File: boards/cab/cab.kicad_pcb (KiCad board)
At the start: 2 copper layers, 71.3 x 71.3 mm, 44 parts, among them J1 Conn_01x08_Female, J2 Conn_01x08_Female, J3 Conn_01x08_Female, J4 Conn_01x08_Female, Q1 SI2308A, Q2 S8550, Q3 BC817-40,215, Q4 S8550, Q5 BC817-40,215, Q6 S8550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

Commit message: Created PCB
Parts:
- removed the Q4 at (229.1, 37.4)
- removed the Q4 at (228.5, 47.9)
- removed the Q6 at (202.0, 71.7)
- removed the Q6 at (238.9, 37.4)
- removed the Q8 at (234.0, 37.4)
- removed the Q8 at (216.9, 59.5)
- removed the U1 at (241.0, 47.2)
- removed the U1 at (247.4, 45.7)
- removed the U2 at (202.9, 77.0)
- removed the U2 at (238.9, 45.7)
- added Q4: S8550, Package_TO_SOT_SMD:SOT-23, F.Cu at (231.9, 145.4)
- added Q6: S8550, Package_TO_SOT_SMD:SOT-23, F.Cu at (237.4, 145.3)
- added Q8: S8550, Package_TO_SOT_SMD:SOT-23, F.Cu at (243.1, 144.9)
- added R10: 50k, Resistor_SMD:R_0805_2012Metric, F.Cu at (192.0, 146.0)
- added R11: 4.7k, Resistor_SMD:R_0805_2012Metric, F.Cu at (177.5, 145.1)
- added SW1: SW_Push, Connector_PinHeader_2.54mm:PinHeader_1x02_P2.54mm_Vertical, F.Cu at (191.1, 151.7)
- added U1: XL1509-ADJ, Package_SO:SOIC-8_3.9x4.9mm_P1.27mm, F.Cu at (236.5, 114.2)
- added U2: XL1509-5.0, Package_SO:SOIC-8_3.9x4.9mm_P1.27mm, F.Cu at (98.4, 44.7)
- L3: footprint StackCabinet:Solenoid -> TerminalBlock_4Ucon:TerminalBlock_4Ucon_1x02_P3.50mm_Vertical
- Q2, Q3, Q5, Q7: footprint Package_TO_SOT_THT:TO-220-3_Vertical -> Package_TO_SOT_SMD:SOT-23
- moved C4 125.2 mm to (100.5, 53.0)
- moved C9 118.9 mm to (171.8, 147.8)
- moved R4 112.4 mm to (239.9, 162.0)
- moved Q7 111.4 mm to (244.9, 157.6)
- moved R5 107.5 mm to (245.4, 162.4)
- moved U3 99.0 mm to (177.4, 150.9)
- moved C2 92.9 mm to (113.5, 44.1), turned to 180 degrees
- moved C8 91.1 mm to (171.9, 151.0)
- moved R3 87.7 mm to (233.1, 162.1)
- moved R6 86.2 mm to (226.7, 149.8)
- moved Q5 85.7 mm to (238.1, 157.4)
- moved C6 84.5 mm to (144.7, 43.6)
- moved R8 82.7 mm to (237.5, 149.3)
- moved Q3 82.5 mm to (233.0, 157.0)
- moved R9 80.0 mm to (243.0, 149.1)
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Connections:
- U3 pad 10: unconnected-(U3-Pad10) -> CAB_STATE
- U3 pad 11: unconnected-(U3-Pad11) -> RxD
- U3 pad 12: unconnected-(U3-Pad12) -> TxD
- U3 pad 13: unconnected-(U3-Pad13) -> 24V_EN
- U3 pad 19: unconnected-(U3-Pad19) -> Net-(U3-Pad19)

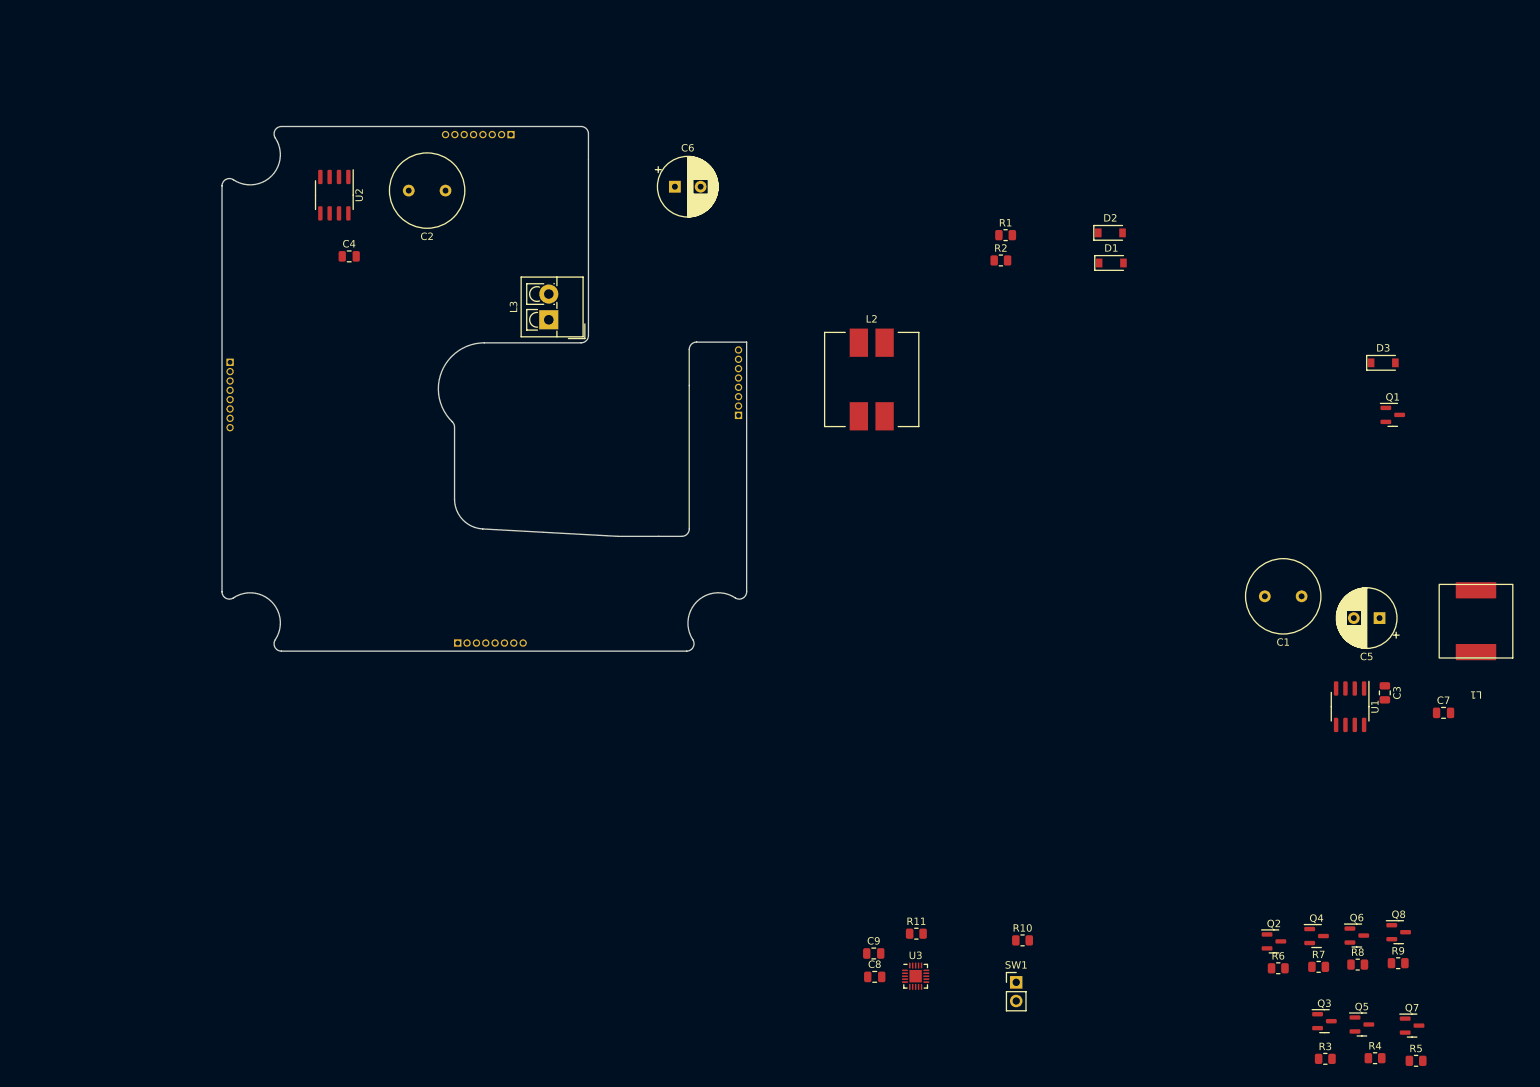
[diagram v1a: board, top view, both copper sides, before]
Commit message: Reworked board outline
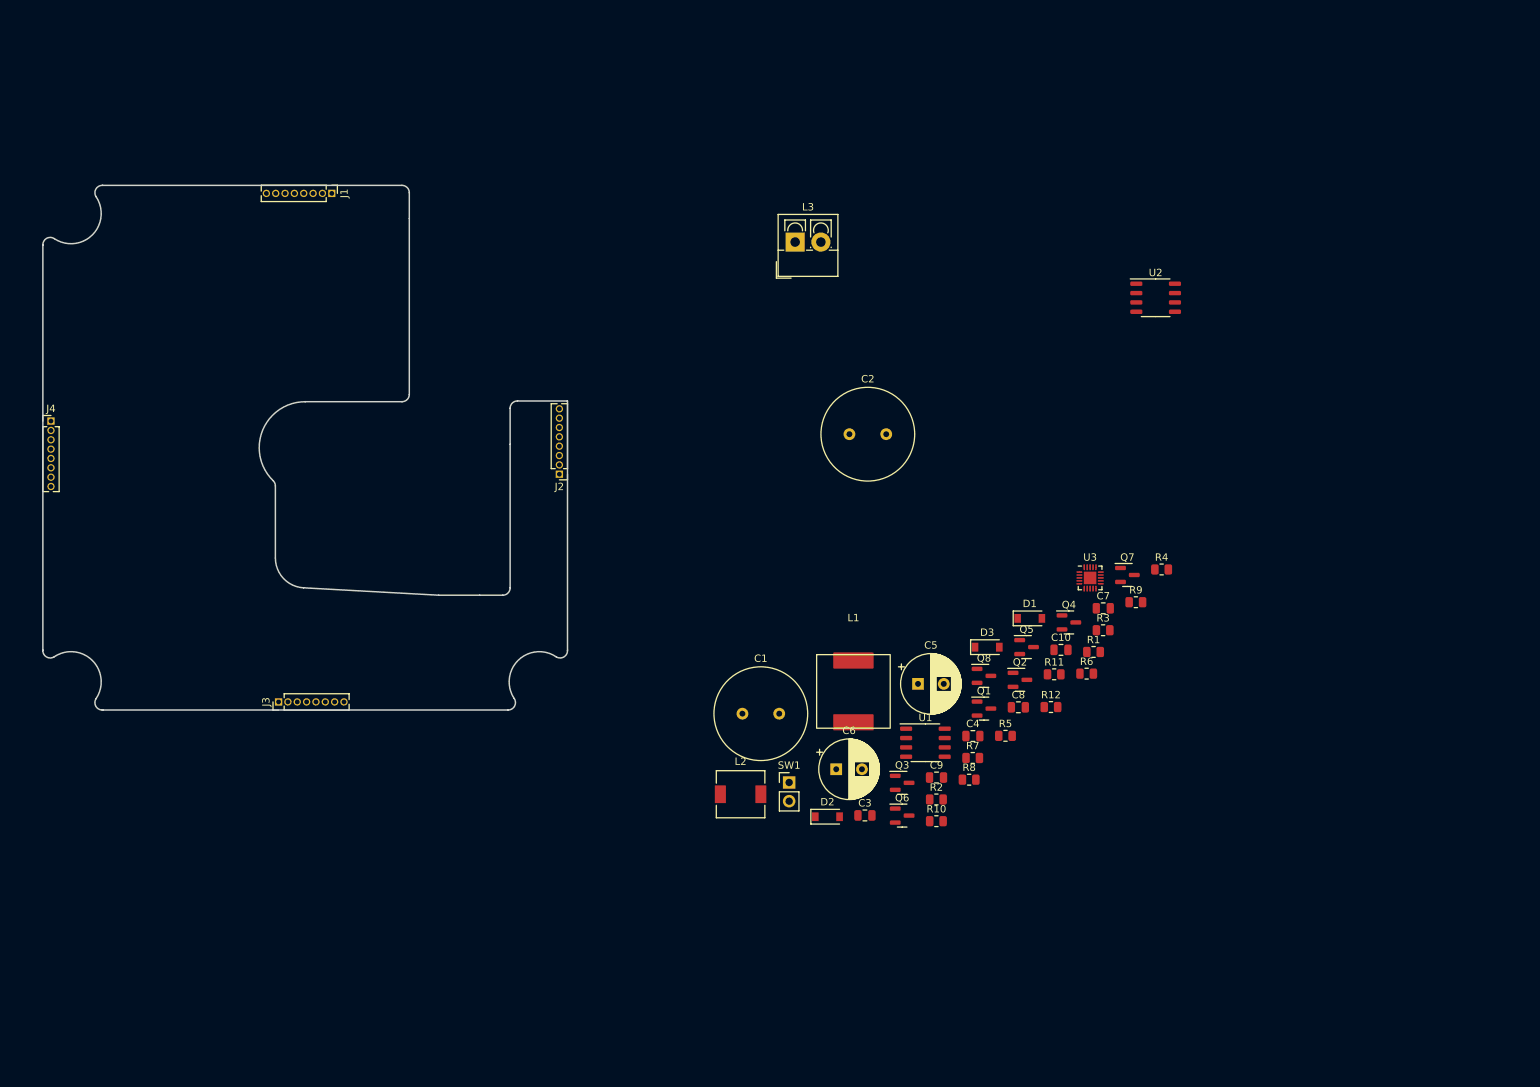
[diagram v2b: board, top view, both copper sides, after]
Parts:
- added C10: 0.1uF, Capacitor_SMD:C_0805_2012Metric, F.Cu at (197.2, 106.5)
- added R12: 1k, Resistor_SMD:R_0805_2012Metric, F.Cu at (195.8, 114.3)
- C1, C2: footprint Capacitor_THT:C_Radial_D10.0mm_H16.0mm_P5.00mm -> Capacitor_THT:C_Radial_D12.5mm_H20.0mm_P5.00mm
- J1, J2, J3, J4: moved to F.Cu
- L2: footprint Inductor_SMD:L_Wuerth_WE-DD-Typ-L-Typ-XL-Typ-XXL -> Inductor_SMD:L_6.3x6.3_H3
- R1: value 50k -> 2.7k
- R2: value 2.7k -> 50k
- U1, U2: footprint Package_SO:SOIC-8_3.9x4.9mm_P1.27mm -> Package_SO:SOP-8_3.9x4.9mm_P1.27mm
- moved U2 112.5 mm to (210.1, 58.7), turned to 0 degrees
- moved C4 106.9 mm to (185.2, 118.2)
- moved D2 88.2 mm to (165.4, 129.2)
- moved L1 85.1 mm to (169.0, 112.2), turned to 0 degrees
- moved C6 82.1 mm to (166.6, 122.8)
- moved C1 77.7 mm to (153.9, 115.2), turned to 0 degrees
- moved R2 73.8 mm to (180.3, 126.9)
- moved C3 72.6 mm to (170.6, 129.0), turned to 0 degrees
- moved R4 72.5 mm to (210.9, 95.6)
- moved Q7 72.4 mm to (206.2, 96.3)
- moved R5 71.2 mm to (189.7, 118.2)
- moved Q5 68.6 mm to (192.5, 106.2)
- moved Q1 68.4 mm to (186.7, 114.5)
- moved D3 66.3 mm to (187.2, 106.2)
- moved Q8 66.3 mm to (186.7, 110.1)
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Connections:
- D2 pad 1: Net-(D2-Pad1) -> 24V
- D2 pad 2: GND -> Net-(D2-Pad2)
- D3 pad 1: 24V -> Net-(D3-Pad1)
- D3 pad 2: Net-(D3-Pad2) -> GND
- L2 pad 1: Net-(D2-Pad1) -> Net-(D3-Pad1)
- L3 pad 2: Net-(D3-Pad2) -> Net-(D2-Pad2)
- Q1 pad 1: SOL_EN -> Net-(Q1-Pad1)
- Q1 pad 3: Net-(D3-Pad2) -> Net-(D2-Pad2)
- Q4 pad 1: Net-(R7-Pad2) -> Net-(Q4-Pad1)
- Q8 pad 1: Net-(R9-Pad2) -> Net-(Q8-Pad1)
- R1 pad 1: FB -> GND
- R1 pad 2: 5V -> FB
- R2 pad 1: GND -> FB
- R2 pad 2: FB -> 5V
- R3 pad 1: R_PWM -> SOL_EN
- R3 pad 2: Net-(Q3-Pad1) -> Net-(Q1-Pad1)
- R4 pad 1: G_PWM -> R_PWM
- R4 pad 2: Net-(Q5-Pad1) -> Net-(Q3-Pad1)
- R5 pad 1: B_PWM -> LED1_PWM
- R5 pad 2: Net-(Q7-Pad1) -> Net-(Q4-Pad1)
- R7 pad 1: LED1_PWM -> G_PWM
- R7 pad 2: Net-(R7-Pad2) -> Net-(Q5-Pad1)
- R9 pad 1: LED3_PWM -> B_PWM
- R9 pad 2: Net-(R9-Pad2) -> Net-(Q7-Pad1)
- U2 pad 2: Net-(D2-Pad1) -> Net-(D3-Pad1)
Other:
- outline, holes or cut-outs redrawn

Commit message: Fixed mosfet footprint
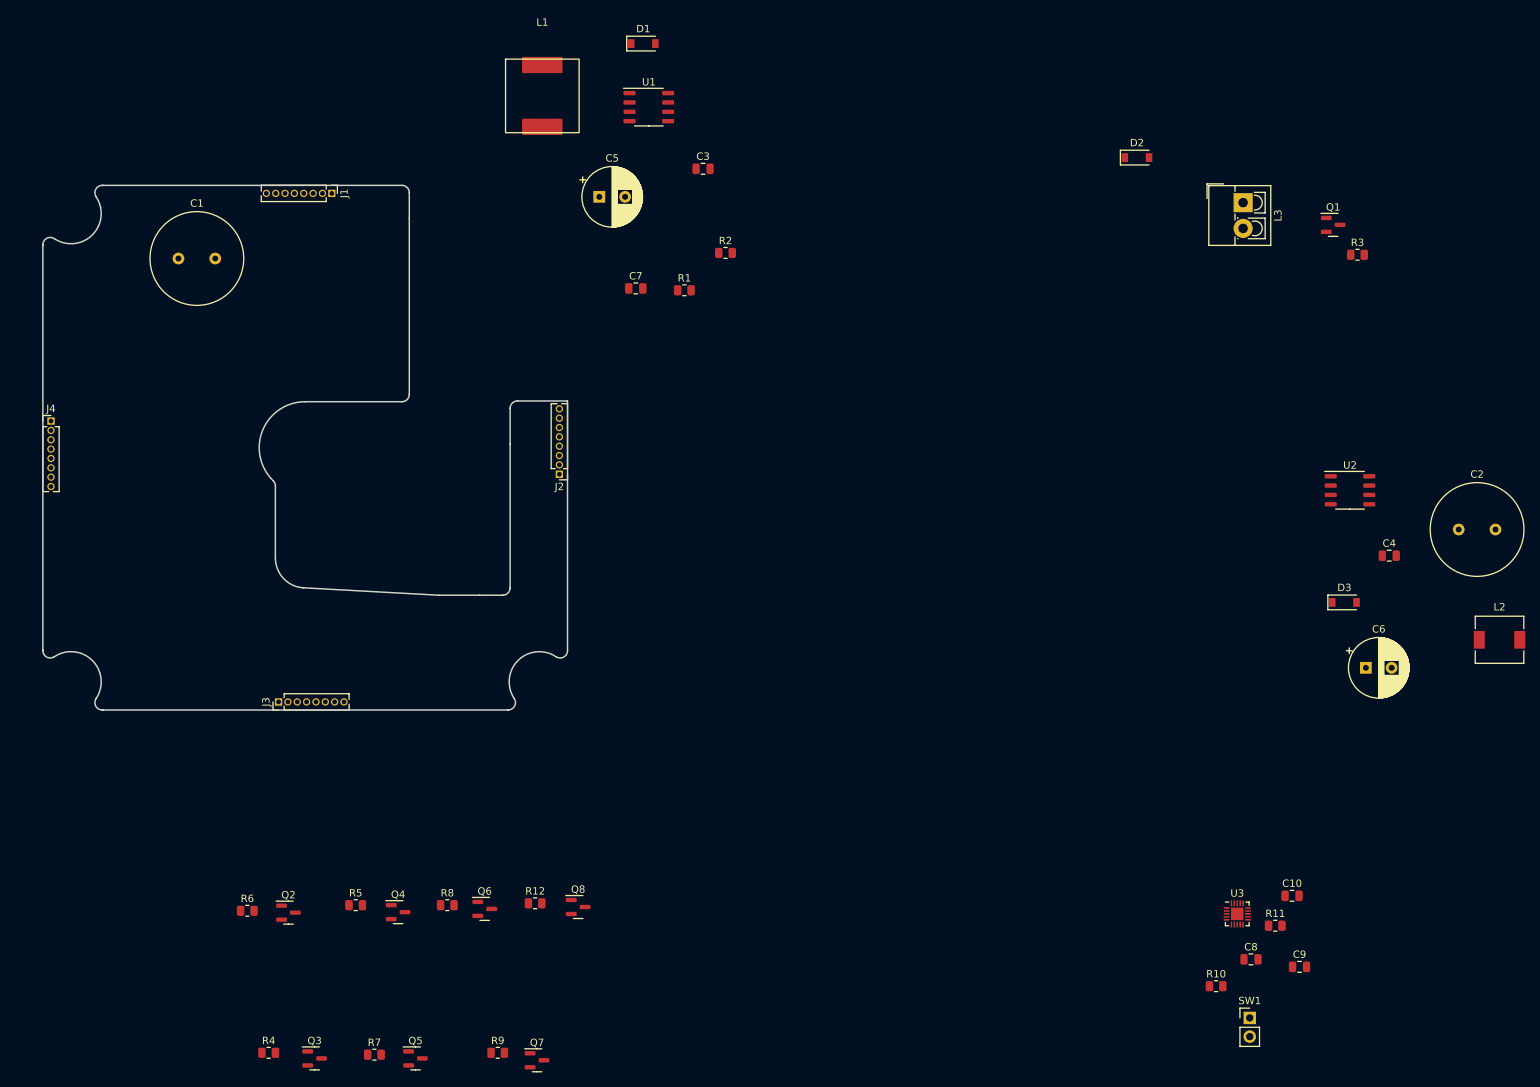
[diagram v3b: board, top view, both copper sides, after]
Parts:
- moved R4 138.0 mm to (89.5, 161.3)
- moved R6 118.5 mm to (86.6, 142.0)
- moved R9 106.2 mm to (120.7, 161.3)
- moved L2 105.3 mm to (256.8, 105.2)
- moved Q2 104.3 mm to (92.2, 142.2)
- moved Q7 103.9 mm to (126.0, 162.3)
- moved Q5 100.1 mm to (109.5, 162.1)
- moved Q4 99.3 mm to (107.1, 142.2)
- moved D2 99.0 mm to (207.5, 39.6)
- moved C1 98.5 mm to (77.3, 53.3)
- moved U1 94.2 mm to (141.2, 32.8)
- moved D1 94.1 mm to (140.4, 24.1)
- moved L1 91.3 mm to (126.7, 31.2)
- moved R5 91.3 mm to (101.3, 141.2)
- moved R7 90.8 mm to (103.9, 161.5)
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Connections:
- Q2 pad 2: LED0 -> 5V
- Q2 pad 3: 5V -> LED0
- Q4 pad 2: LED1 -> 5V
- Q4 pad 3: 5V -> LED1
- Q6 pad 2: LED2 -> 5V
- Q6 pad 3: 5V -> LED2
- Q8 pad 2: LED3 -> 5V
- Q8 pad 3: 5V -> LED3

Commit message: Placed Power, Attiny and LED power
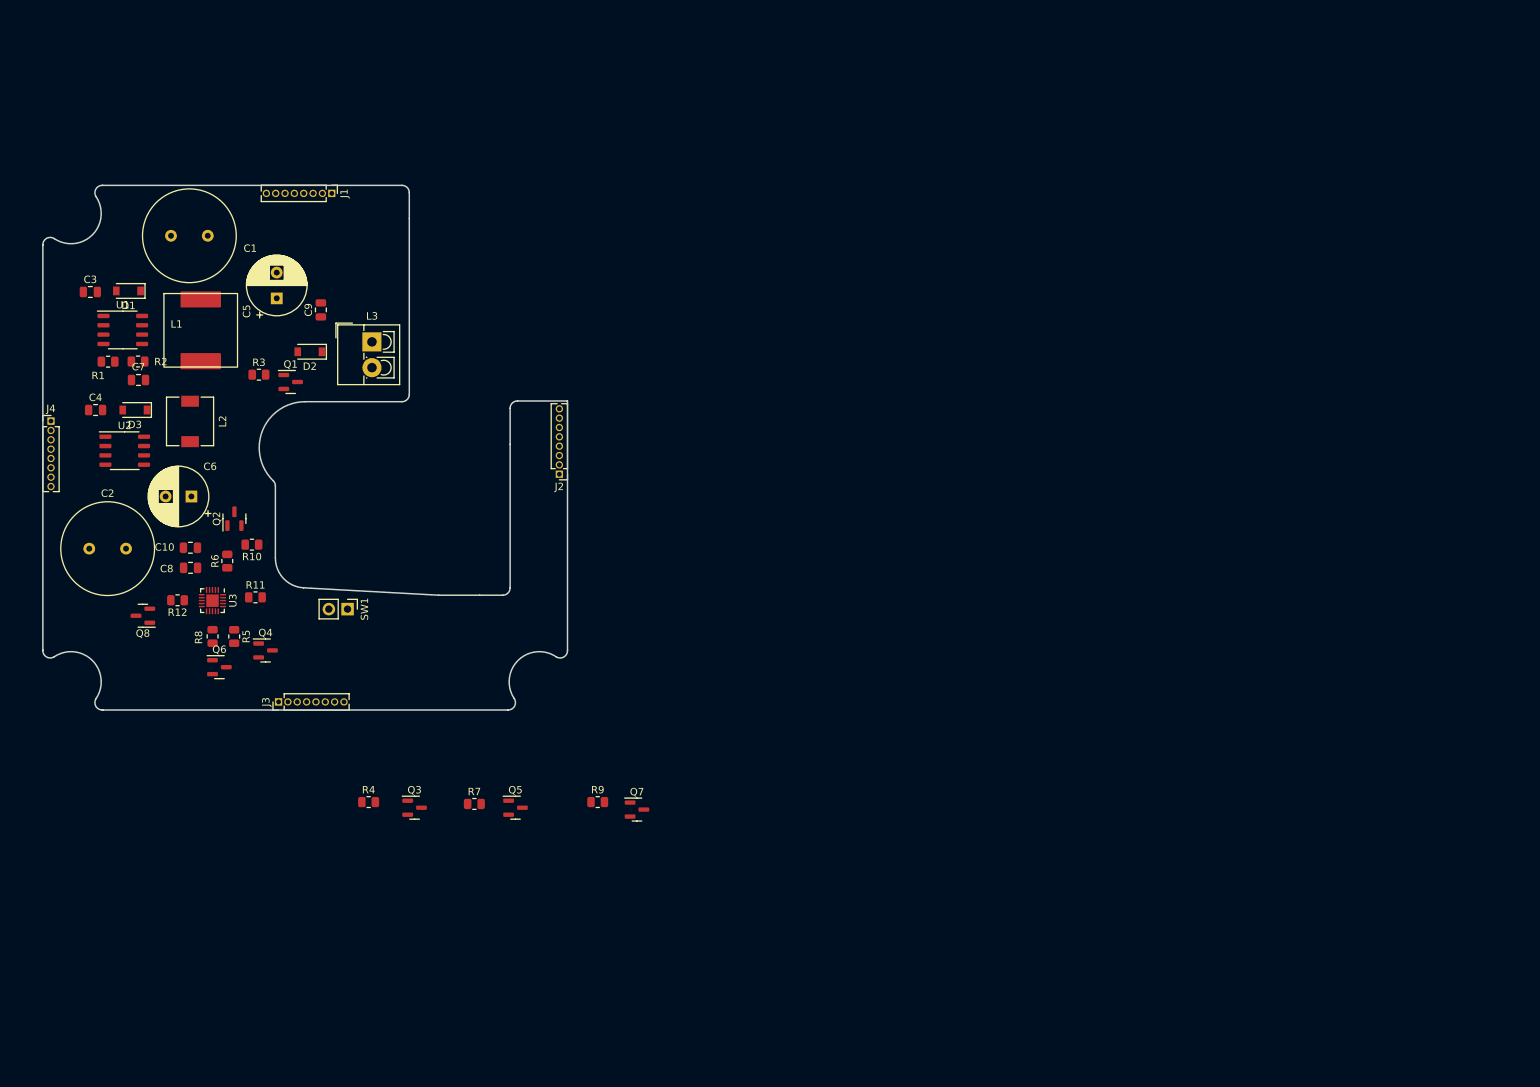
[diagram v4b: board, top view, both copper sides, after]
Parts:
- moved C2 186.1 mm to (65.1, 92.8)
- moved L2 180.4 mm to (78.8, 75.5), turned to -90 degrees
- moved C4 176.9 mm to (66.0, 73.9)
- moved U2 166.6 mm to (70.0, 79.5)
- moved D3 166.4 mm to (71.3, 73.9), turned to 180 degrees
- moved C6 161.3 mm to (79.0, 85.7), turned to 180 degrees
- moved C9 160.2 mm to (96.6, 60.3), turned to 90 degrees
- moved C10 157.0 mm to (78.9, 92.7), turned to 180 degrees
- moved C8 153.6 mm to (78.9, 95.4), turned to 180 degrees
- moved R3 150.2 mm to (88.2, 69.1)
- moved U3 145.6 mm to (81.9, 99.8), turned to -90 degrees
- moved R11 145.6 mm to (87.7, 99.4)
- moved R10 144.1 mm to (87.2, 92.2), turned to 180 degrees
- moved Q1 143.3 mm to (92.5, 70.1)
- moved SW1 134.6 mm to (100.2, 101.0), turned to -90 degrees
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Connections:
- C5 pad 1: 5V -> 24V
- C6 pad 1: 24V -> 5V
- C7 pad 1: 5V -> 24V
- L1 pad 2: 5V -> 24V
- L2 pad 2: 24V -> 5V
- R2 pad 2: 5V -> 24V
- U2 pad 3: 24V -> 5V
- U3 pad 1: R_PWM -> SOL_EN
- U3 pad 12: TxD -> GDA
- U3 pad 13: 24V_EN -> LED2_PWM
- U3 pad 14: SOL_EN -> LED1_PWM
- U3 pad 2: G_PWM -> 24V_EN
- U3 pad 6: LED1_PWM -> R_PWM
- U3 pad 7: LED2_PWM -> G_PWM

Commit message: Routing & planes
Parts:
- moved Q7 64.7 mm to (78.8, 105.8), turned to -90 degrees
- moved R9 61.0 mm to (79.0, 101.4), turned to -90 degrees
- moved Q5 44.4 mm to (84.6, 105.9), turned to -90 degrees
- moved Q3 42.3 mm to (73.3, 105.8), turned to -90 degrees
- moved R7 41.9 mm to (84.7, 101.4), turned to -90 degrees
- moved R4 39.4 mm to (73.4, 101.4), turned to -90 degrees
- moved SW1 30.7 mm to (96.9, 70.5)
- moved Q2 15.5 mm to (76.2, 101.6), turned to -90 degrees
- moved R11 11.6 mm to (88.5, 87.8), turned to 90 degrees
- moved R10 9.62 mm to (78.4, 88.5), turned to 90 degrees
- moved R6 8.70 mm to (76.2, 98.5), turned to 0 degrees
- moved C8 8.57 mm to (82.0, 87.4), turned to 0 degrees
- moved Q6 7.35 mm to (81.8, 101.6), turned to -90 degrees
- moved U3 6.90 mm to (81.9, 92.9)
- moved R5 6.73 mm to (87.5, 98.5), turned to 0 degrees
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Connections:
- net Net-(D2-Pad2) renamed /SOL_R
- U3 pad 1: SOL_EN -> 24V_EN
- U3 pad 10: CAB_STATE -> LED2_PWM
- U3 pad 13: LED2_PWM -> G_PWM
- U3 pad 2: 24V_EN -> unconnected-(U3-Pad2)
- U3 pad 20: LED0_PWM -> SOL_EN
- U3 pad 5: B_PWM -> CAB_STATE
- U3 pad 6: R_PWM -> LED3_PWM
- U3 pad 7: G_PWM -> R_PWM
- U3 pad 8: LED3_PWM -> LED0_PWM
- U3 pad 9: unconnected-(U3-Pad9) -> B_PWM
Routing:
- net G: track 0.00 -> 179.1 mm, vias 0 -> 3
- net B: track 0.00 -> 178.4 mm, vias 0 -> 4
- net R: track 0.00 -> 177.6 mm, vias 0 -> 3
- net GDA: track 0.00 -> 175.3 mm, vias 0 -> 4
- net LED0: track 0.00 -> 85.0 mm, vias 0 -> 4
- net SEL1: track 0.00 -> 70.1 mm, vias 0 -> 2
- net LED1: track 0.00 -> 63.5 mm, vias 0 -> 3
- net SEL0: track 0.00 -> 58.2 mm, vias 0 -> 1
- net 5V: track 0.00 -> 53.9 mm, vias 0 -> 7
- net 24V_EN: track 0.00 -> 47.8 mm, vias 0 -> 2
- net CAB_STATE: track 0.00 -> 37.8 mm, vias 0 -> 2
- net LED3: track 0.00 -> 36.6 mm, vias 0 -> 2
- net SEL3: track 0.00 -> 36.4 mm, vias 0 -> 2
- net SOL_EN: track 0.00 -> 29.0 mm
- net SEL2: track 0.00 -> 27.9 mm, vias 0 -> 2
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- added copper zone on F.Cu, net /SOL_R
- added copper zone on F.Cu, net 24V
- added copper zone on F.Cu, net 5V
- added copper zone on B.Cu, net GND
- added copper zone on F.Cu, net GND
- added copper zone on F.Cu, net VBUS

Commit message: Tuned polygons
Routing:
- net GND: track 0.00 -> 3.57 mm
- net 5V: track 53.9 -> 57.3 mm
